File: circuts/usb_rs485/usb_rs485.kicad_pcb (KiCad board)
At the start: 2 copper layers, 11 parts, among them CON1 USB-MINI-B, IC1 SP3481CN, P2 CONN_2, U1 CP2102

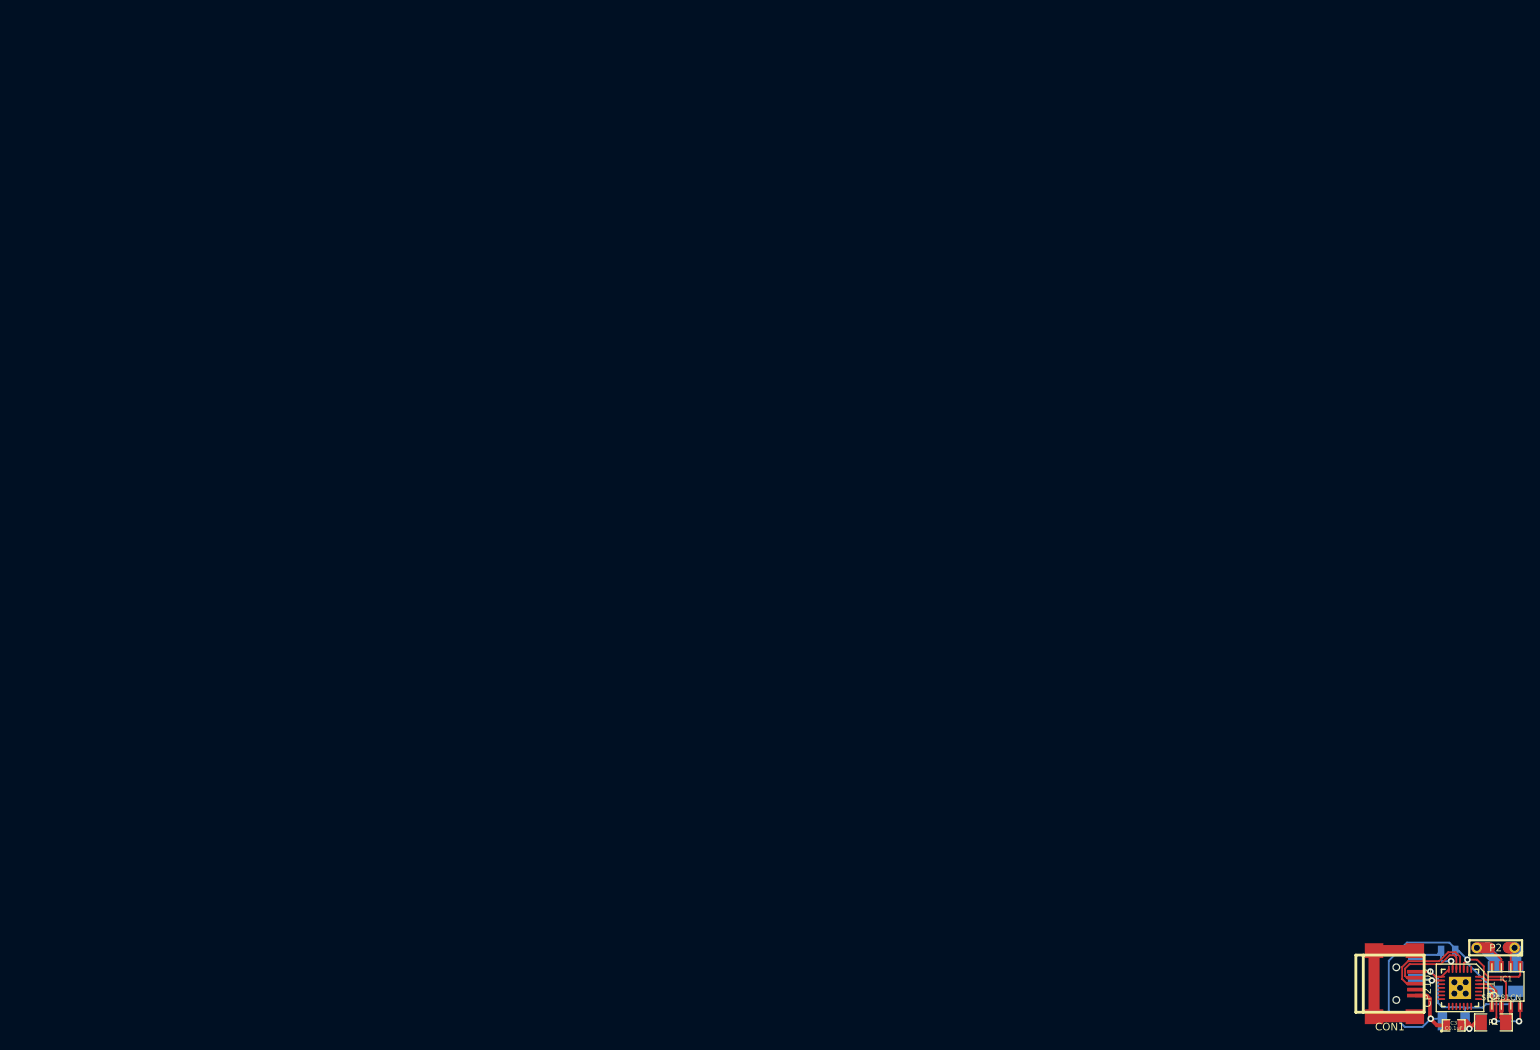
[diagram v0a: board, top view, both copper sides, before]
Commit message: Added submodule, fixed pcb and added rename.sh
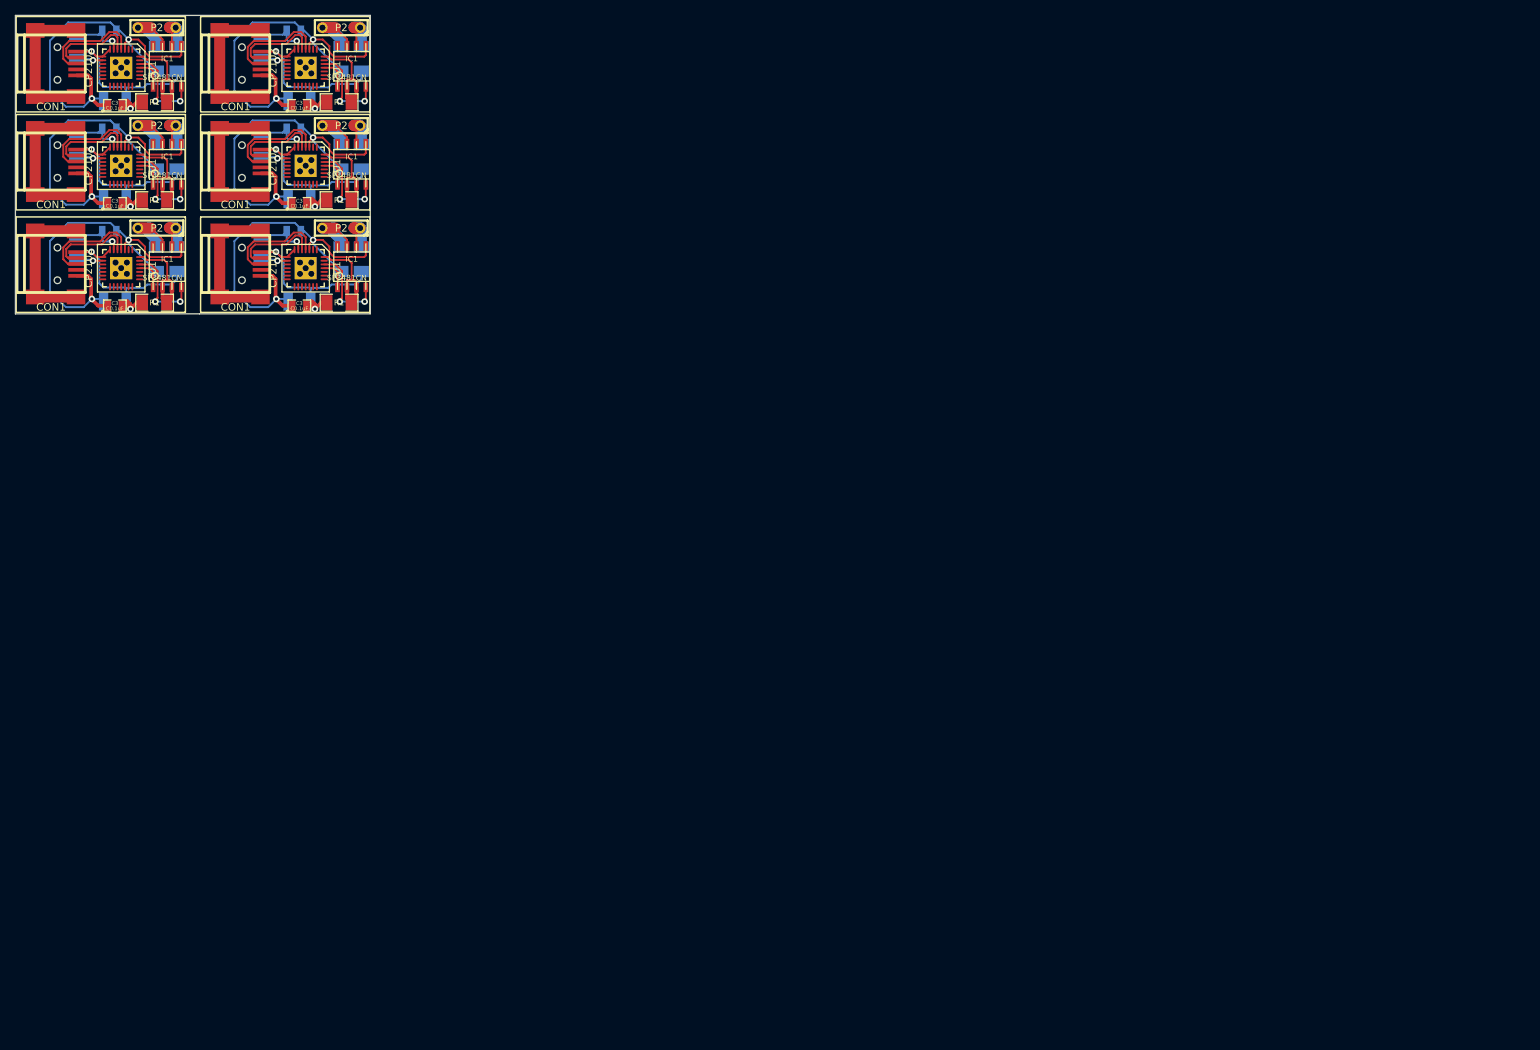
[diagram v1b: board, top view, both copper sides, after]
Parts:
- added C1: C0.1uF, SM0805, B.Cu at (37.5, 29.1)
- added C1: C0.1uF, SM0805, B.Cu at (12.7, 29.1)
- added C1: C0.1uF, SM0805, B.Cu at (12.7, 15.2)
- added C1: C0.1uF, SM0805, B.Cu at (37.5, 15.2)
- added C1: C0.1uF, SM0805, B.Cu at (37.5, 2.05)
- added C2: C1.0uF, SM1210, B.Cu at (38.2, 38.5)
- added C2: C1.0uF, SM1210, B.Cu at (13.4, 38.5)
- added C2: C1.0uF, SM1210, B.Cu at (13.4, 24.7)
- added C2: C1.0uF, SM1210, B.Cu at (38.2, 24.7)
- added C2: C1.0uF, SM1210, B.Cu at (38.2, 11.5)
- added C3: C0.1uF, SM0805, F.Cu at (38.2, 39.1)
- added C3: C0.1uF, SM0805, F.Cu at (13.4, 39.1)
- added C3: C0.1uF, SM0805, F.Cu at (13.4, 25.3)
- added C3: C0.1uF, SM0805, F.Cu at (38.2, 25.3)
- added C3: C0.1uF, SM0805, F.Cu at (38.2, 12.1)
- added CON1: USB-MINI-B, USB_MINI_B, F.Cu at (29.7, 33.5)
- added CON1: USB-MINI-B, USB_MINI_B, F.Cu at (4.82, 33.5)
- added CON1: USB-MINI-B, USB_MINI_B, F.Cu at (4.82, 19.7)
- added CON1: USB-MINI-B, USB_MINI_B, F.Cu at (29.7, 19.7)
- added CON1: USB-MINI-B, USB_MINI_B, F.Cu at (29.7, 6.48)
- added IC1: SP3481CN, so-8, F.Cu at (45.3, 33.9)
- added IC1: SP3481CN, so-8, F.Cu at (20.4, 33.9)
- added IC1: SP3481CN, so-8, F.Cu at (20.4, 20.1)
- added IC1: SP3481CN, so-8, F.Cu at (45.3, 20.1)
- added IC1: SP3481CN, so-8, F.Cu at (45.3, 6.85)
- added P2: CONN_2, C2, F.Cu at (43.9, 28.6)
- added P2: CONN_2, C2, F.Cu at (19.1, 28.6)
- added P2: CONN_2, C2, F.Cu at (19.1, 14.8)
- added P2: CONN_2, C2, F.Cu at (43.9, 14.8)
- added P2: CONN_2, C2, F.Cu at (43.9, 1.65)
- added R1: 10K, SM1206, F.Cu at (43.6, 38.7)
- added R1: 10K, SM1206, F.Cu at (18.8, 38.7)
- added R1: 10K, SM1206, F.Cu at (18.8, 24.9)
- added R1: 10K, SM1206, F.Cu at (43.6, 24.9)
- added R1: 10K, SM1206, F.Cu at (43.6, 11.7)
- added R2: 560, SM1206, B.Cu at (46.6, 32.9)
- added R2: 560, SM1206, B.Cu at (21.8, 32.9)
- added R2: 560, SM1206, B.Cu at (21.8, 19.1)
- added R2: 560, SM1206, B.Cu at (46.6, 19.1)
- added R2: 560, SM1206, B.Cu at (46.6, 5.85)
- added R3: 560, SM1206, B.Cu at (43.9, 32.9)
- added R3: 560, SM1206, B.Cu at (19.0, 32.9)
- added R3: 560, SM1206, B.Cu at (19.0, 19.1)
- added R3: 560, SM1206, B.Cu at (43.9, 19.1)
- added R3: 560, SM1206, B.Cu at (43.9, 5.85)
- added R4: K4.7, SM1206, B.Cu at (33.1, 31.2)
- added R4: K4.7, SM1206, B.Cu at (8.25, 31.2)
- added R4: K4.7, SM1206, B.Cu at (8.25, 17.4)
- added R4: K4.7, SM1206, B.Cu at (33.1, 17.4)
- added R4: K4.7, SM1206, B.Cu at (33.1, 4.25)
- added U1: CP2102, QFN28, F.Cu at (39.1, 34.0)
- added U1: CP2102, QFN28, F.Cu at (14.2, 34.0)
- added U1: CP2102, QFN28, F.Cu at (14.2, 20.2)
- added U1: CP2102, QFN28, F.Cu at (39.1, 20.2)
- added U1: CP2102, QFN28, F.Cu at (39.1, 7.05)
- moved IC1 218.8 mm to (20.4, 6.85)
- moved C1 218.8 mm to (12.7, 2.05)
- moved C2 218.8 mm to (13.4, 11.5)
- moved C3 218.8 mm to (13.4, 12.1)
- moved CON1 218.8 mm to (4.82, 6.48)
- moved P2 218.8 mm to (19.1, 1.65)
- moved R1 218.8 mm to (18.8, 11.7)
- moved R2 218.8 mm to (21.8, 5.85)
- moved R3 218.8 mm to (19.0, 5.85)
- moved R4 218.8 mm to (8.25, 4.25)
- moved U1 218.8 mm to (14.2, 7.05)
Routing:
- net GND: track 53.1 -> 318.6 mm, vias 2 -> 12
- net /VBUS: track 30.4 -> 182.5 mm, vias 2 -> 12
- net N-0000030: track 19.9 -> 119.4 mm
- net /D+: track 14.3 -> 85.5 mm
- net N-000002: track 14.1 -> 84.5 mm
- net N-000008: track 12.3 -> 73.9 mm, vias 2 -> 12
- net /D-: track 11.9 -> 71.3 mm
- net N-000005: track 9.39 -> 56.3 mm
- net /VDD: track 7.75 -> 46.5 mm, vias 1 -> 6
- net N-000004: track 6.95 -> 41.7 mm, vias 1 -> 6
- net /RX: track 4.10 -> 24.6 mm
- net N-0000010: track 3.56 -> 21.4 mm, vias 1 -> 6
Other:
- board outline added: 47.8 x 40.2 mm

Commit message: For sending to iteadstudio.com
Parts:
- removed the C1 at (37.5, 29.1)
- removed the C1 at (12.7, 29.1)
- removed the C2 at (38.2, 38.5)
- removed the C2 at (13.4, 38.5)
- removed the C3 at (38.2, 39.1)
- removed the C3 at (13.4, 39.1)
- removed the CON1 at (29.7, 33.5)
- removed the CON1 at (4.82, 33.5)
- removed the IC1 at (45.3, 33.9)
- removed the IC1 at (20.4, 33.9)
- removed the P2 at (43.9, 28.6)
- removed the P2 at (19.1, 28.6)
- removed the R1 at (43.6, 38.7)
- removed the R1 at (18.8, 38.7)
- removed the R2 at (46.6, 32.9)
- removed the R2 at (21.8, 32.9)
- removed the R3 at (43.9, 32.9)
- removed the R3 at (19.0, 32.9)
- removed the R4 at (33.1, 31.2)
- removed the R4 at (8.25, 31.2)
- removed the U1 at (39.1, 34.0)
- removed the U1 at (14.2, 34.0)
- moved CON1 1.20 mm to (4.82, 20.9)
- moved CON1 1.20 mm to (29.7, 20.9)
- moved R1 1.20 mm to (18.8, 26.1)
- moved R1 1.20 mm to (43.6, 26.1)
- moved P2 1.20 mm to (19.1, 16.1)
- moved P2 1.20 mm to (43.9, 16.1)
- moved C1 1.20 mm to (12.7, 16.4)
- moved C1 1.20 mm to (37.5, 16.4)
- moved C2 1.20 mm to (13.4, 25.9)
- moved C2 1.20 mm to (38.2, 25.9)
- moved C3 1.20 mm to (13.4, 26.5)
- moved C3 1.20 mm to (38.2, 26.5)
- moved IC1 1.20 mm to (20.4, 21.2)
- moved IC1 1.20 mm to (45.3, 21.2)
- moved R2 1.20 mm to (21.8, 20.2)
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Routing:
- net GND: track 318.6 -> 212.4 mm, vias 12 -> 8
- net /VBUS: track 182.5 -> 121.7 mm, vias 12 -> 8
- net N-0000030: track 119.4 -> 79.6 mm
- net /D+: track 85.5 -> 57.0 mm
- net N-000002: track 84.5 -> 56.4 mm
- net N-000008: track 73.9 -> 49.3 mm, vias 12 -> 8
- net /D-: track 71.3 -> 47.5 mm
- net N-000005: track 56.3 -> 37.6 mm
- net /VDD: track 46.5 -> 31.0 mm, vias 6 -> 4
- net N-000004: track 41.7 -> 27.8 mm, vias 6 -> 4
- net /RX: track 24.6 -> 16.4 mm
- net N-0000010: track 21.4 -> 14.3 mm, vias 6 -> 4
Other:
- board size 47.8 x 40.2 mm -> 47.8 x 27.6 mm
